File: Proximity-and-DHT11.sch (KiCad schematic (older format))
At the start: 18 parts, among them P1 Power, P2 Analog, P3 Digital, P4 Digital, P5 CONN_01X01, P6 CONN_01X01, P7 CONN_01X01, P8 CONN_01X01

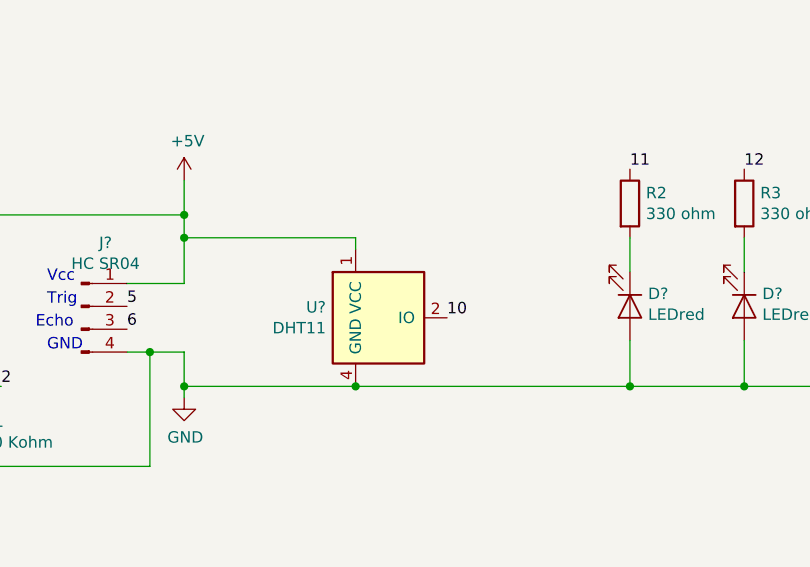
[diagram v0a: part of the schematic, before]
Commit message: Aggiunto potenziometro
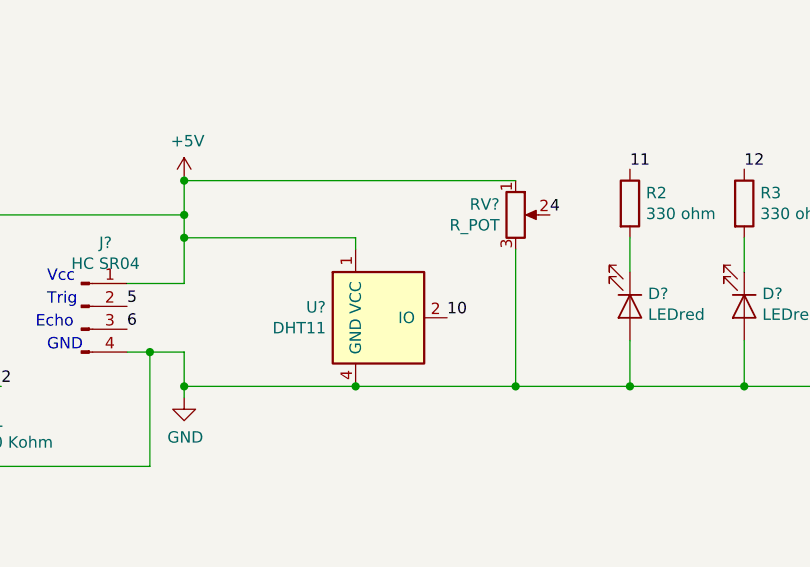
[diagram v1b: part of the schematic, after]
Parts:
- added RV?: R_POT, symbol Device:R_POT
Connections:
- net +5V: now also RV?.1
- net 4: now also RV?.2
- net GND: now also RV?.3
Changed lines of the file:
@@
 Connection ~ 4000 2250
 Wire Wire Line
-	4000 2250 2800 2250
+	4000 2250 3500 2250
 Text Label 4000 1300 0    50   ~ 0
 11
@@
 Text Label 5000 1300 0    50   ~ 0
 13
+$Comp
+L Device:R_POT RV?
+U 1 1 5C866EDB
+P 3500 1500
+F 0 "RV?" H 3430 1546 50  0000 R CNN
+F 1 "R_POT" H 3430 1455 50  0000 R CNN
+F 2 "" H 3500 1500 50  0001 C CNN
+F 3 "~" H 3500 1500 50  0001 C CNN
+	1    3500 1500
+	1    0    0    -1
+$EndComp
+Wire Wire Line
+	3500 1350 2050 1350
+Connection ~ 2050 1350
+Wire Wire Line
+	3500 1650 3500 2250
+Connection ~ 3500 2250
+Wire Wire Line
+	3500 2250 2800 2250
+Text Label 3650 1500 0    50   ~ 0
+4
 $EndSCHEMATC
